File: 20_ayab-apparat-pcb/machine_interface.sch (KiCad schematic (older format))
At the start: 12 parts, among them K1 CONN_3, K2 CONN_3, P1 CONN_4, P2 CONN_10, P3 CONN_10, P4 CONN_8, P5 CONN_5, P6 CONN_5, U2 PCF8574, U3 PCF8574, U4 ULN2803, U5 ULN2803

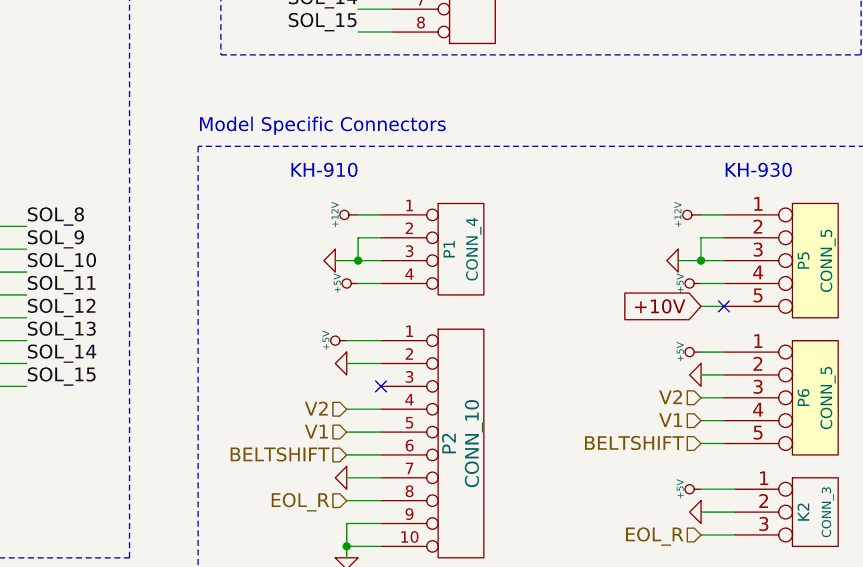
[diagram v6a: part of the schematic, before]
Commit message: Added automatic switching between ATmega and original machine control when VUSB is attached
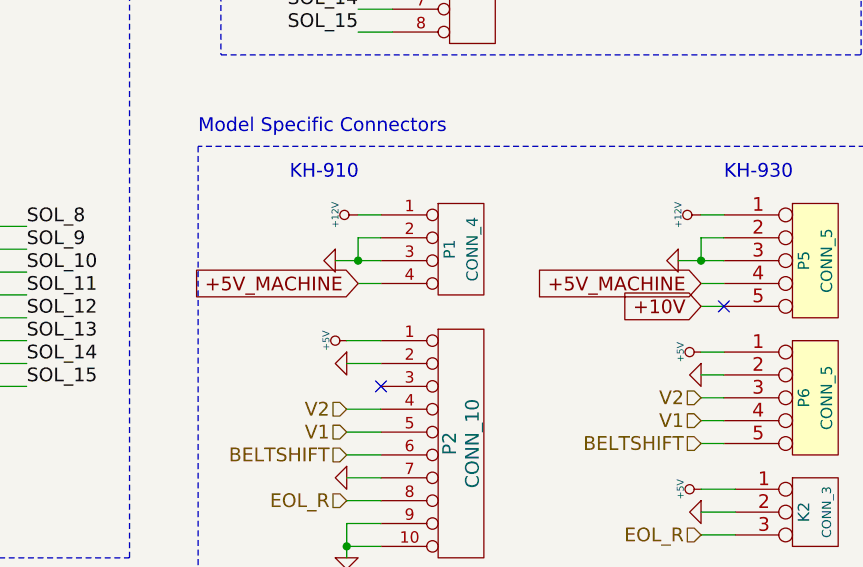
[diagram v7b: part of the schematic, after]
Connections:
- net +5V: no longer P1.4 (P4), P5.4
- new net +5V_MACHINE: P1.4 (P4), P5.4
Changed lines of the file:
@@
 EOL_L
 $Comp
-L +5V #PWR05
+L +5V #PWR08
 U 1 1 52E1540D
 P 7650 1550
-F 0 "#PWR05" H 7650 1640 20  0001 C CNN
+F 0 "#PWR08" H 7650 1640 20  0001 C CNN
 F 1 "+5V" H 7650 1640 30  0000 C CNN
 F 2 "" H 7650 1550 60  0000 C CNN
@@
 $EndComp
 $Comp
-L GND #PWR06
+L GND #PWR09
 U 1 1 52E15421
 P 7650 1650
-F 0 "#PWR06" H 7650 1650 30  0001 C CNN
+F 0 "#PWR09" H 7650 1650 30  0001 C CNN
 F 1 "GND" H 7650 1580 30  0001 C CNN
 F 2 "" H 7650 1650 60  0000 C CNN
@@
 $EndComp
 $Comp
-L GND #PWR07
+L GND #PWR010
 U 1 1 52E15472
 P 6300 4200
-F 0 "#PWR07" H 6300 4200 30  0001 C CNN
+F 0 "#PWR010" H 6300 4200 30  0001 C CNN
 F 1 "GND" H 6300 4130 30  0001 C CNN
 F 2 "" H 6300 4200 60  0000 C CNN
@@
 	1    6300 4200
 	0    1    1    0
-$EndComp
-$Comp
-L +5V #PWR08
-U 1 1 52E15500
-P 6400 4300
-F 0 "#PWR08" H 6400 4390 20  0001 C CNN
-F 1 "+5V" H 6400 4390 30  0000 C CNN
-F 2 "" H 6400 4300 60  0000 C CNN
-F 3 "" H 6400 4300 60  0000 C CNN
-	1    6400 4300
-	0    -1   -1   0
 $EndComp
 Text Notes 6100 3850 0    60   ~ 0
@@
 $EndComp
 $Comp
-L GND #PWR09
+L GND #PWR011
 U 1 1 52E1590C
 P 3800 3350
-F 0 "#PWR09" H 3800 3350 30  0001 C CNN
+F 0 "#PWR011" H 3800 3350 30  0001 C CNN
 F 1 "GND" H 3800 3280 30  0001 C CNN
 F 2 "" H 3800 3350 60  0000 C CNN
@@
 $EndComp
 $Comp
-L GND #PWR010
+L GND #PWR012
 U 1 1 52E15921
 P 3800 5150
-F 0 "#PWR010" H 3800 5150 30  0001 C CNN
+F 0 "#PWR012" H 3800 5150 30  0001 C CNN
 F 1 "GND" H 3800 5080 30  0001 C CNN
 F 2 "" H 3800 5150 60  0000 C CNN
@@
 $EndComp
 $Comp
-L GND #PWR011
+L GND #PWR013
 U 1 1 52E6C9F8
 P 1400 3200
-F 0 "#PWR011" H 1400 3200 30  0001 C CNN
+F 0 "#PWR013" H 1400 3200 30  0001 C CNN
 F 1 "GND" H 1400 3130 30  0001 C CNN
 F 2 "" H 1400 3200 60  0000 C CNN
@@
 $EndComp
 $Comp
-L +5V #PWR012
+L +5V #PWR014
 U 1 1 52E6CA3F
 P 1400 2900
-F 0 "#PWR012" H 1400 2990 20  0001 C CNN
+F 0 "#PWR014" H 1400 2990 20  0001 C CNN
 F 1 "+5V" H 1400 2990 30  0000 C CNN
 F 2 "" H 1400 2900 60  0000 C CNN
@@
 $EndComp
 $Comp
-L GND #PWR013
+L GND #PWR015
 U 1 1 52E6CA86
 P 1400 2800
-F 0 "#PWR013" H 1400 2800 30  0001 C CNN
+F 0 "#PWR015" H 1400 2800 30  0001 C CNN
 F 1 "GND" H 1400 2730 30  0001 C CNN
 F 2 "" H 1400 2800 60  0000 C CNN
@@
 $EndComp
 $Comp
-L GND #PWR014
+L GND #PWR016
 U 1 1 52E6CB3E
 P 1400 5000
-F 0 "#PWR014" H 1400 5000 30  0001 C CNN
+F 0 "#PWR016" H 1400 5000 30  0001 C CNN
 F 1 "GND" H 1400 4930 30  0001 C CNN
 F 2 "" H 1400 5000 60  0000 C CNN
@@
 $EndComp
 $Comp
-L GND #PWR015
+L GND #PWR017
 U 1 1 52E6CB52
 P 1400 4600
-F 0 "#PWR015" H 1400 4600 30  0001 C CNN
+F 0 "#PWR017" H 1400 4600 30  0001 C CNN
 F 1 "GND" H 1400 4530 30  0001 C CNN
 F 2 "" H 1400 4600 60  0000 C CNN
@@
 $EndComp
 $Comp
-L +5V #PWR016
+L +5V #PWR018
 U 1 1 52E6CB66
 P 1400 4700
-F 0 "#PWR016" H 1400 4790 20  0001 C CNN
+F 0 "#PWR018" H 1400 4790 20  0001 C CNN
 F 1 "+5V" H 1400 4790 30  0000 C CNN
 F 2 "" H 1400 4700 60  0000 C CNN
@@
 $EndComp
 $Comp
-L +5V #PWR017
+L +5V #PWR019
 U 1 1 52E6CB7A
 P 1400 4350
-F 0 "#PWR017" H 1400 4440 20  0001 C CNN
+F 0 "#PWR019" H 1400 4440 20  0001 C CNN
 F 1 "+5V" H 1400 4440 30  0000 C CNN
 F 2 "" H 1400 4350 60  0000 C CNN
@@
 SCL
 $Comp
-L +5V #PWR018
+L +5V #PWR020
 U 1 1 52E6CE5D
 P 6350 4550
-F 0 "#PWR018" H 6350 4640 20  0001 C CNN
+F 0 "#PWR020" H 6350 4640 20  0001 C CNN
 F 1 "+5V" H 6350 4640 30  0000 C CNN
 F 2 "" H 6350 4550 60  0000 C CNN
@@
 $EndComp
 $Comp
-L GND #PWR019
+L GND #PWR021
 U 1 1 52E6CE71
 P 6350 4650
-F 0 "#PWR019" H 6350 4650 30  0001 C CNN
+F 0 "#PWR021" H 6350 4650 30  0001 C CNN
 F 1 "GND" H 6350 4580 30  0001 C CNN
 F 2 "" H 6350 4650 60  0000 C CNN
@@
 $EndComp
 $Comp
-L GND #PWR020
+L GND #PWR022
 U 1 1 52E6CE94
 P 6350 5500
-F 0 "#PWR020" H 6350 5500 30  0001 C CNN
+F 0 "#PWR022" H 6350 5500 30  0001 C CNN
 F 1 "GND" H 6350 5430 30  0001 C CNN
 F 2 "" H 6350 5500 60  0000 C CNN
@@
 $EndComp
 $Comp
-L GND #PWR021
+L GND #PWR023
 U 1 1 52E6CF37
 P 6350 5150
-F 0 "#PWR021" H 6350 5150 30  0001 C CNN
+F 0 "#PWR023" H 6350 5150 30  0001 C CNN
 F 1 "GND" H 6350 5080 30  0001 C CNN
 F 2 "" H 6350 5150 60  0000 C CNN
@@
 Model Specific Connectors
 $Comp
-L GND #PWR022
+L GND #PWR024
 U 1 1 52E7E76D
 P 7800 4200
-F 0 "#PWR022" H 7800 4200 30  0001 C CNN
+F 0 "#PWR024" H 7800 4200 30  0001 C CNN
 F 1 "GND" H 7800 4130 30  0001 C CNN
 F 2 "" H 7800 4200 60  0000 C CNN
@@
 	0    1    1    0
 $EndComp
-$Comp
-L +5V #PWR023
-U 1 1 52E7E781
-P 7900 4300
-F 0 "#PWR023" H 7900 4390 20  0001 C CNN
-F 1 "+5V" H 7900 4390 30  0000 C CNN
-F 2 "" H 7900 4300 60  0000 C CNN
-F 3 "" H 7900 4300 60  0000 C CNN
-	1    7900 4300
-	0    -1   -1   0
-$EndComp
 Wire Wire Line
 	7800 4200 8000 4200
@@
 	7900 4400 8000 4400
 $Comp
-L +5V #PWR024
+L +5V #PWR025
 U 1 1 52E7EA73
 P 7900 5200
-F 0 "#PWR024" H 7900 5290 20  0001 C CNN
+F 0 "#PWR025" H 7900 5290 20  0001 C CNN
 F 1 "+5V" H 7900 5290 30  0000 C CNN
 F 2 "" H 7900 5200 60  0000 C CNN
@@
 $EndComp
 $Comp
-L GND #PWR025
+L GND #PWR026
 U 1 1 52E7EA87
 P 7900 5300
-F 0 "#PWR025" H 7900 5300 30  0001 C CNN
+F 0 "#PWR026" H 7900 5300 30  0001 C CNN
 F 1 "GND" H 7900 5230 30  0001 C CNN
 F 2 "" H 7900 5300 60  0000 C CNN
@@
 	7900 5200 8050 5200
 $Comp
-L +5V #PWR026
+L +5V #PWR027
 U 1 1 52E7ECB1
 P 7900 4600
-F 0 "#PWR026" H 7900 4690 20  0001 C CNN
+F 0 "#PWR027" H 7900 4690 20  0001 C CNN
 F 1 "+5V" H 7900 4690 30  0000 C CNN
 F 2 "" H 7900 4600 60  0000 C CNN
@@
 $EndComp
 $Comp
-L GND #PWR027
+L GND #PWR028
 U 1 1 52E7ECD1
 P 7900 4700
-F 0 "#PWR027" H 7900 4700 30  0001 C CNN
+F 0 "#PWR028" H 7900 4700 30  0001 C CNN
 F 1 "GND" H 7900 4630 30  0001 C CNN
 F 2 "" H 7900 4700 60  0000 C CNN
@@
 	8600 1150 5800 1150
 $Comp
-L +12V #PWR028
+L +12V #PWR029
 U 1 1 52EA8D08
 P 6400 4000
-F 0 "#PWR028" H 6400 3950 20  0001 C CNN
+F 0 "#PWR029" H 6400 3950 20  0001 C CNN
 F 1 "+12V" H 6400 4100 30  0000 C CNN
 F 2 "" H 6400 4000 60  0000 C CNN
@@
 $EndComp
 $Comp
-L +12V #PWR029
+L +12V #PWR030
 U 1 1 52EA8D1C
 P 7900 4000
-F 0 "#PWR029" H 7900 3950 20  0001 C CNN
+F 0 "#PWR030" H 7900 3950 20  0001 C CNN
 F 1 "+12V" H 7900 4100 30  0000 C CNN
 F 2 "" H 7900 4000 60  0000 C CNN
@@
 $EndComp
 $Comp
-L +12V #PWR030
+L +12V #PWR031
 U 1 1 52EA8D30
 P 6350 1450
-F 0 "#PWR030" H 6350 1400 20  0001 C CNN
+F 0 "#PWR031" H 6350 1400 20  0001 C CNN
 F 1 "+12V" H 6350 1550 30  0000 C CNN
 F 2 "" H 6350 1450 60  0000 C CNN
@@
 $EndComp
 $Comp
-L +12V #PWR031
+L +12V #PWR032
 U 1 1 52EA8D44
 P 3600 1850
-F 0 "#PWR031" H 3600 1800 20  0001 C CNN
+F 0 "#PWR032" H 3600 1800 20  0001 C CNN
 F 1 "+12V" H 3600 1950 30  0000 C CNN
 F 2 "" H 3600 1850 60  0000 C CNN
@@
 $EndComp
 $Comp
-L +12V #PWR032
+L +12V #PWR033
 U 1 1 52EA8D58
 P 3650 3650
-F 0 "#PWR032" H 3650 3600 20  0001 C CNN
+F 0 "#PWR033" H 3650 3600 20  0001 C CNN
 F 1 "+12V" H 3650 3750 30  0000 C CNN
 F 2 "" H 3650 3650 60  0000 C CNN
@@
 NoConn ~ 2800 4950
 NoConn ~ 6500 4750
+Text GLabel 7900 4300 0    60   Input ~ 0
++5V_MACHINE
+Text GLabel 6400 4300 0    60   Input ~ 0
++5V_MACHINE
 $EndSCHEMATC
